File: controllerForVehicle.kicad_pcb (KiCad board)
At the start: 4 copper layers, 208 parts, among them IC1 MP2338GTL-Z, J1 Debug, J10 Conn_01x02, J11 Conn_01x02, J12 Conn_01x02, J13 USB_C_Receptacle_PowerOnly_6P, J14 USB_C_Receptacle_USB2.0_16P, J15 USB_C_Receptacle_USB2.0_16P, J2 Boot_Sel, J3 VIN, J4 Conn_01x08, J5 Conn_01x08, J6 Conn_01x08, J7 Conn_01x02, J8 Conn_01x02, J9 Conn_01x02, SW1 RESET, SW2 IO0, SW3 EN, T1 S8050, T2 S8050, U1 STM32F103C8Tx, U10 MPU6050, U11 MCP23S17_SO, U2 L298N, U3 L298N, U4 L298N, U5 ESP32-WROOM-32D, U6 CP2102N-Axx-xQFN28, U7 L7805, U8 AMS1117-3.3, U9 PCA9685PW, Y1 8mHz, Y2 32.768kHz

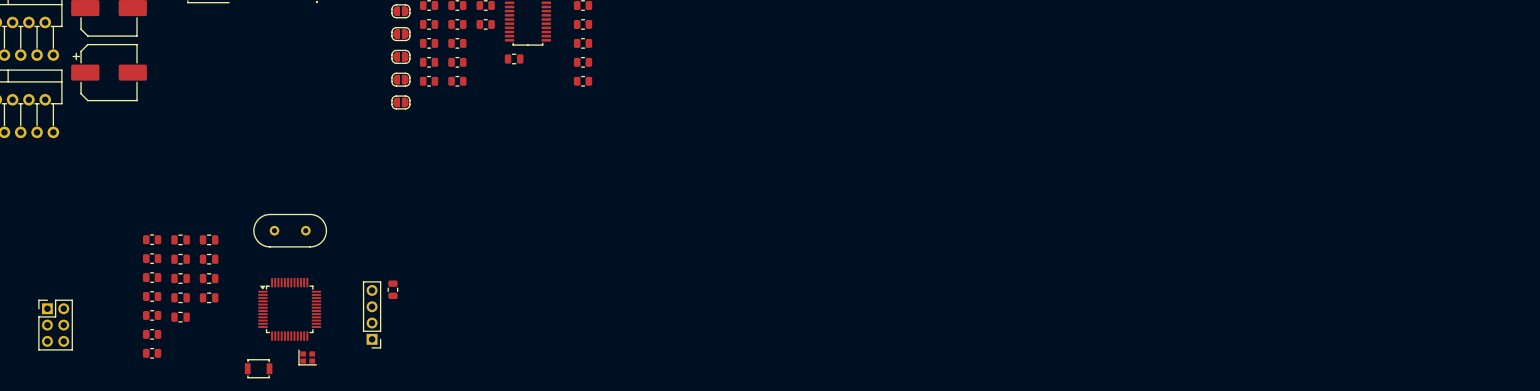
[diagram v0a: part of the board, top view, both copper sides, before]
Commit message: Routing
Routing STM32 and Components
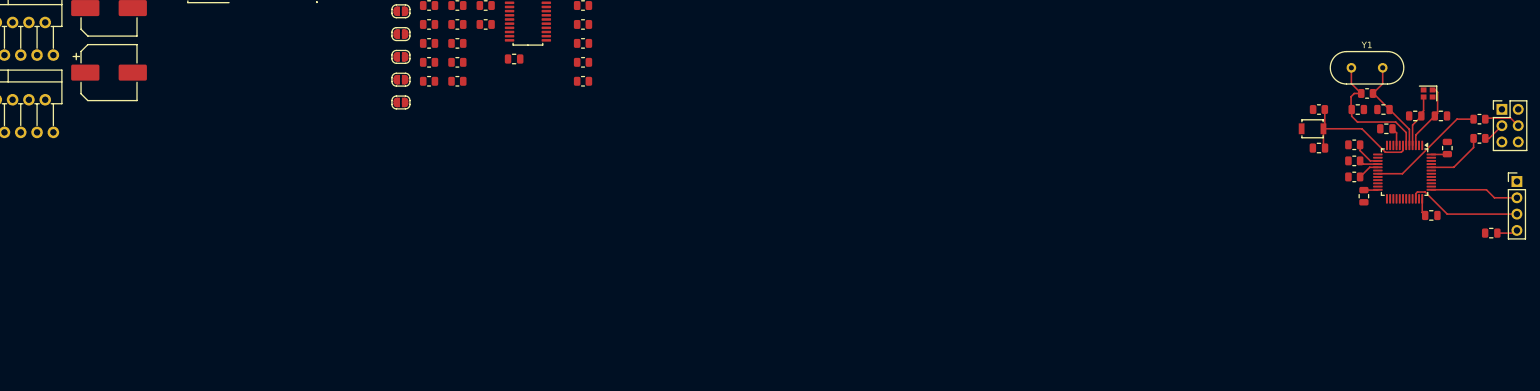
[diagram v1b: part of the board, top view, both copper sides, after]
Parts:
- Y1: footprint Crystal:Crystal_HC49-U_Vertical -> Crystal:Crystal_HC49-4H_Vertical
- moved J2 228.7 mm to (269.7, 138.2)
- moved R7 209.9 mm to (266.2, 139.8), turned to 180 degrees
- moved R6 209.0 mm to (266.2, 142.8)
- moved C5 199.1 mm to (261.2, 144.2), turned to -90 degrees
- moved C4 195.2 mm to (258.7, 154.8), turned to 180 degrees
- moved C7 193.2 mm to (260.2, 139.2)
- moved R1 190.6 mm to (248.7, 135.8), turned to 180 degrees
- moved C8 189.6 mm to (256.2, 139.2)
- moved C2 188.9 mm to (251.7, 141.2)
- moved C1 188.5 mm to (251.2, 138.2), turned to 180 degrees
- moved R4 188.2 mm to (246.7, 148.8), turned to 180 degrees
- moved R3 188.1 mm to (246.7, 146.2), turned to 180 degrees
- moved R2 188.1 mm to (246.7, 143.8), turned to 180 degrees
- moved C3 184.8 mm to (248.2, 151.8), turned to 90 degrees
- moved R5 184.6 mm to (241.2, 138.2)
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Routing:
- net OSC_OUT: track 0.00 -> 21.1 mm
- net RESET: track 0.00 -> 20.7 mm
- net BOOT1: track 0.00 -> 18.4 mm
- net SWDIO: track 0.00 -> 18.1 mm
- net OSC_IN: track 0.00 -> 15.1 mm
- net SWCLK: track 0.00 -> 13.9 mm
- net 3V3: track 0.00 -> 13.6 mm
- net PC14: track 0.00 -> 10.6 mm
- net BOOT0: track 0.00 -> 9.28 mm
- net PC15: track 0.00 -> 8.25 mm
- net Net-(J2-Pad4): track 0.00 -> 5.68 mm
- net Net-(U1-PA5): track 0.00 -> 4.33 mm
- net Net-(J2-Pad3): track 0.00 -> 3.41 mm
- net Net-(U1-PA7): track 0.00 -> 3.38 mm
- net Net-(U1-PA6): track 0.00 -> 2.97 mm

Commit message: Routing
Routing ESP32 and Components
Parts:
- removed C7, C8: 20p, Capacitor_SMD:C_0805_2012Metric
- removed Y2: 32.768kHz, Crystal:Crystal_SMD_2016-4Pin_2.0x1.6mm
- moved C16 220.6 mm to (246.0, 61.8)
- moved C19 220.5 mm to (249.8, 56.5), turned to 90 degrees
- moved C17 215.8 mm to (246.0, 59.4)
- moved C20 213.0 mm to (247.4, 56.5), turned to 90 degrees
- moved C21 209.7 mm to (245.1, 82.0)
- moved U6 203.2 mm to (242.8, 54.5), turned to 90 degrees
- moved C15 181.2 mm to (205.5, 52.5), turned to 90 degrees
- moved C14 177.3 mm to (202.0, 52.5), turned to 90 degrees
- moved C18 174.5 mm to (204.3, 61.2)
- moved R17 170.8 mm to (251.1, 36.9)
- moved R18 170.8 mm to (251.1, 39.9)
- moved U5 170.8 mm to (219.7, 58.1)
- moved SW2 169.1 mm to (245.1, 79.0), turned to 180 degrees
- moved R11 168.1 mm to (241.1, 76.0)
- moved R8 165.7 mm to (236.3, 77.1), turned to 90 degrees
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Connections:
- U1 pad 3: PC14 -> unconnected-(U1-PC14-Pad3)
- U1 pad 4: PC15 -> unconnected-(U1-PC15-Pad4)
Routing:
- net IO0: track 0.00 -> 19.0 mm
- net 3V3: track 13.6 -> 28.4 mm
- net EN: track 0.00 -> 11.1 mm
- net OSC_OUT: track 21.1 -> 10.5 mm
- net PC14: track 10.6 -> 0.00 mm
- net PC15: track 8.25 -> 0.00 mm
- net Net-(C22-Pad1): track 0.00 -> 7.13 mm
- net Net-(C21-Pad1): track 0.00 -> 6.89 mm
- net DTR: track 0.00 -> 6.13 mm
- net RTS: track 0.00 -> 5.93 mm
- net 5V1: track 0.00 -> 4.78 mm
- net Net-(T1-B): track 0.00 -> 4.76 mm
- net OSC_IN: track 15.1 -> 11.0 mm
- net Net-(U6-TXD): track 0.00 -> 3.28 mm
- net RXD: track 0.00 -> 3.24 mm
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
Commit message: Routing ESP32 and Components
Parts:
- removed R10: 470R, Resistor_SMD:R_0805_2012Metric
- removed R17: 0R (NC), Resistor_SMD:R_0805_2012Metric
- removed R18: 0R(NC), Resistor_SMD:R_0805_2012Metric
- moved J14 85.7 mm to (185.2, 80.1), turned to -90 degrees
- moved D27 82.6 mm to (193.4, 79.2), turned to -90 degrees
- moved D28 82.6 mm to (193.4, 81.0), turned to 90 degrees
- moved D26 70.8 mm to (186.4, 73.1), turned to 180 degrees
- moved R45 61.6 mm to (190.9, 81.9), turned to -90 degrees
- moved R47 60.0 mm to (190.9, 78.3), turned to 90 degrees
- moved C19 59.0 mm to (200.7, 89.2), turned to 180 degrees
- moved C16 57.3 mm to (193.8, 85.4), turned to -90 degrees
- moved R49 56.8 mm to (191.6, 75.4), turned to 180 degrees
- moved C17 56.3 mm to (196.1, 85.4), turned to -90 degrees
- moved C20 55.8 mm to (200.7, 87.0), turned to 180 degrees
- moved U6 50.3 mm to (200.9, 82.2), turned to 0 degrees
- moved R16 41.5 mm to (206.9, 82.3), turned to 0 degrees
- moved R15 35.4 mm to (206.9, 80.2), turned to 0 degrees
- moved SW2 34.7 mm to (214.0, 63.7), turned to 90 degrees
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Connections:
- U6 pad 26: Net-(U6-TXD) -> TXD
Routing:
- net EN: track 11.1 -> 41.2 mm, vias 0 -> 2
- net Net-(D26-A): track 0.00 -> 13.0 mm
- net ESP_D+: track 0.00 -> 11.7 mm
- net IO0: track 19.0 -> 29.5 mm
- net ESP_D-: track 0.00 -> 9.32 mm
- net TXD: track 1.98 -> 8.65 mm
- net Net-(J14-D--PadA7): track 0.00 -> 6.24 mm
- net Net-(J14-D+-PadA6): track 0.00 -> 6.18 mm, vias 0 -> 2
- net RXD: track 3.24 -> 9.36 mm
- net 5V1: track 4.78 -> 10.2 mm
- net Net-(T2-B): track 2.28 -> 7.00 mm
- net Net-(U6-TXD): track 3.28 -> 0.00 mm
- net RTS: track 5.93 -> 7.75 mm, vias 0 -> 2
- net Net-(C21-Pad1): track 6.89 -> 5.14 mm
- net Net-(C22-Pad1): track 7.13 -> 5.43 mm
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
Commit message: Power Routing
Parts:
- removed R62, R63, R64: 12k, Resistor_SMD:R_0805_2012Metric
- added R10: 12k, Resistor_SMD:R_0805_2012Metric, F.Cu at (-21.2, 83.8)
- added R17: 12k, Resistor_SMD:R_0805_2012Metric, F.Cu at (-21.2, 86.8)
- added R18: 12k, Resistor_SMD:R_0805_2012Metric, F.Cu at (-7.89, 73.8)
- moved C30 174.9 mm to (171.0, 236.2)
- moved C28 174.5 mm to (163.0, 235.2), turned to 180 degrees
- moved C31 174.3 mm to (171.0, 238.4)
- moved C29 170.8 mm to (166.2, 231.6), turned to 90 degrees
- moved C27 169.1 mm to (163.0, 237.6), turned to 180 degrees
- moved C33 163.6 mm to (158.7, 227.8), turned to -90 degrees
- moved R25 162.5 mm to (159.2, 235.2), turned to 180 degrees
- moved R27 159.7 mm to (159.2, 237.6), turned to 180 degrees
- moved C32 158.7 mm to (163.2, 227.8), turned to -90 degrees
- moved R26 158.4 mm to (165.8, 227.8), turned to -90 degrees
- moved R30 152.6 mm to (160.9, 227.8), turned to -90 degrees
- moved R29 152.3 mm to (156.4, 227.8), turned to -90 degrees
- moved R28 151.6 mm to (158.4, 231.0), turned to 180 degrees
- moved J3 150.4 mm to (33.8, 185.1)
- moved C23 146.3 mm to (119.8, 223.8), turned to 90 degrees
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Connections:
- R58 pad 1: DCEn6 -> Net-(U3-EnB)
- R58 pad 2: Net-(U9-LED10) -> DCEn4
- R59 pad 1: DCEn5 -> Net-(U4-EnA)
- R59 pad 2: Net-(U9-LED11) -> DCEn5
- R60 pad 1: DCEn4 -> Net-(U4-EnB)
- R60 pad 2: Net-(U9-LED12) -> DCEn6
- U2 pad 11: DCEn2 -> Net-(U2-EnB)
- U2 pad 6: DCEn1 -> Net-(U2-EnA)
- U3 pad 11: DCEn4 -> Net-(U3-EnB)
- U3 pad 6: DCEn3 -> Net-(U3-EnA)
- U4 pad 11: DCEn6 -> Net-(U4-EnB)
- U4 pad 6: DCEn5 -> Net-(U4-EnA)
- U9 pad 17: Net-(U9-LED10) -> DCEn6
- U9 pad 18: Net-(U9-LED11) -> DCEn5
- U9 pad 19: Net-(U9-LED12) -> DCEn4
- U9 pad 20: Net-(U9-LED13) -> DCEn3
- U9 pad 21: Net-(U9-LED14) -> DCEn2
- U9 pad 22: Net-(U9-LED15) -> DCEn1

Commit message: Reapply "placing completed."
This reverts commit 83f85ef5575867dc78eeeae3514badb4960c2205.
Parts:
- added C7: 220uF 35V, Capacitor_SMD:CP_Elec_8x10.5, F.Cu at (-20.6, 32.5)
- moved R55 276.9 mm to (343.0, 143.3)
- moved R83 274.5 mm to (-150.8, 52.7), turned to 90 degrees
- moved R53 273.4 mm to (339.7, 139.3), turned to -90 degrees
- moved R82 271.4 mm to (-148.2, 52.6), turned to 90 degrees
- moved R52 271.0 mm to (337.6, 139.3), turned to -90 degrees
- moved R81 267.2 mm to (-144.4, 52.4), turned to 90 degrees
- moved R80 264.3 mm to (-141.9, 52.4), turned to 90 degrees
- moved C43 255.7 mm to (334.1, 137.8), turned to 180 degrees
- moved U9 249.6 mm to (331.9, 144.3)
- moved J8 238.8 mm to (-150.2, 39.1), turned to 180 degrees
- moved R79 234.6 mm to (-113.0, 50.7), turned to 90 degrees
- moved R78 231.4 mm to (-110.4, 50.7), turned to 90 degrees
- moved R68 230.4 mm to (339.3, 120.8), turned to 90 degrees
- moved JP7 229.1 mm to (340.0, 116.5), turned to -90 degrees
- moved R72 227.0 mm to (337.2, 120.8), turned to 90 degrees
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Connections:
- J9 pad 1: DC5_2 -> DC4_2
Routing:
- net DC2_1: track 0.00 -> 18.9 mm
- net DC2_2: track 0.00 -> 14.6 mm
- net DCIn6_1: track 0.00 -> 14.1 mm
- net DCIn6_2: track 0.00 -> 14.0 mm
- net Net-(U4-EnA): track 0.00 -> 10.4 mm
- net DCIn5_2: track 0.00 -> 9.16 mm
- net Net-(U2-EnA): track 0.00 -> 9.10 mm
- net DCIn1_2: track 0.00 -> 7.60 mm
- net DCIn1_1: track 0.00 -> 7.58 mm
- net Net-(U4-EnB): track 0.00 -> 5.49 mm

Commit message: silinecek
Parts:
- removed D32, D33, D34, D35, D36, D37, D38, D39: 1N4007, Diode_SMD:D_SOD-123
- removed R82, R83: 100R, Resistor_SMD:R_0805_2012Metric
- removed R84: 10K, Resistor_SMD:R_0805_2012Metric
- added C8: 0.1u, Capacitor_SMD:C_0805_2012Metric, F.Cu at (-17.1, 7.30)
- added D17: 1N4007, Diode_SMD:D_SOD-123, F.Cu at (-30.6, -20.7)
- added D18: 1N4007, Diode_SMD:D_SOD-123, F.Cu at (-30.6, -17.4)
- added D19: 1N4007, Diode_SMD:D_SOD-123, F.Cu at (-30.6, -14.0)
- added D20: 1N4007, Diode_SMD:D_SOD-123, F.Cu at (-30.6, -10.7)
- added D21: 1N4007, Diode_SMD:D_SOD-123, F.Cu at (-30.6, -7.33)
- added D22: 1N4007, Diode_SMD:D_SOD-123, F.Cu at (-30.6, -3.98)
- added D23: 1N4007, Diode_SMD:D_SOD-123, F.Cu at (-30.6, -0.62)
- added D24: 1N4007, Diode_SMD:D_SOD-123, F.Cu at (-30.6, 2.73)
- added J16: Servo6, Connector_JST:JST_XA_B03B-XASK-1_1x03_P2.50mm_Vertical, F.Cu at (105.1, 38.6)
- added J17: Servo8, Connector_JST:JST_XA_B03B-XASK-1_1x03_P2.50mm_Vertical, F.Cu at (105.2, 61.4)
- added J18: USB_C_Receptacle_PowerOnly_6P, Connector_USB:USB_C_Receptacle_GCT_USB4125-xx-x_6P_TopMnt_Horizontal, F.Cu at (-8.29, -0.62)
- added J19: USB_C_Receptacle_USB2.0_16P, Connector_USB:USB_C_Receptacle_Palconn_UTC16-G, F.Cu at (-20.0, -18.3)
- added J20: USB_C_Receptacle_USB2.0_16P, Connector_USB:USB_C_Receptacle_Palconn_UTC16-G, F.Cu at (-20.0, -8.30)
- added R62: 10k, Resistor_SMD:R_0805_2012Metric, F.Cu at (36.0, 20.0)
- added R63: 10k, Resistor_SMD:R_0805_2012Metric, F.Cu at (-23.6, 7.28)
- added R64: 10k, Resistor_SMD:R_0805_2012Metric, F.Cu at (-23.6, 10.2)
- C10: value 0.1u -> 220uF 35V; footprint Capacitor_SMD:C_0805_2012Metric -> Capacitor_SMD:CP_Elec_8x10.5
- C12: value 220uF 35V -> 100u; footprint Capacitor_SMD:CP_Elec_8x10.5 -> Capacitor_SMD:C_0805_2012Metric
- C13: value 220uF 35V -> 0.1u; footprint Capacitor_SMD:CP_Elec_8x10.5 -> Capacitor_SMD:C_0805_2012Metric
- C14: value 100u -> 10u
- C16, C19: value 10u -> 1n / 50V
- C17: value 0.1u -> 10u
- C18: value 1n / 50V -> 0.1u
- C20: value 0.1u -> 1n / 50V
- C21, C22: value 1n / 50V -> 10u
- C25: value 10u -> 22u
- C26: value 10u -> 0.1u
- C27: value 22u -> 0.1u
- C28, C29: value 0.1u -> 22u
- C30: value 22u -> 22n
- C31: value 22u -> 300p
- C32: value 22n -> 0.01u
- C33: value 300p -> 47u
- C34: value 0.01u -> 47u
- C35, C36: value 47u -> 4.7u
- C37: value 4.7u -> 0.01u
- C38: value 4.7u -> 2200p
- C39: value 0.01u -> 22p
- C40: value 2200p -> 0.01u
- C41: value 22p -> 220uF 35V; footprint Capacitor_SMD:C_0805_2012Metric -> Capacitor_SMD:CP_Elec_8x10.5
- C42: value 0.01u -> 220uF 35V; footprint Capacitor_SMD:C_0805_2012Metric -> Capacitor_SMD:CP_Elec_8x10.5
- C7: value 220uF 35V -> 1uf; footprint Capacitor_SMD:CP_Elec_8x10.5 -> Capacitor_SMD:C_0805_2012Metric
- C9: value 1uf -> 220uF 35V; footprint Capacitor_SMD:C_0805_2012Metric -> Capacitor_SMD:CP_Elec_8x10.5
- D27: value ESD05V88D-LC -> 1N5819; footprint Diode_SMD:D_SOD-882 -> Diode_SMD:D_SOD-123
- D31: value 1N5819 -> ESD05V88D-LC; footprint Diode_SMD:D_SOD-123 -> Diode_SMD:D_SOD-882
- J10, J11, J12, J8, J9: footprint Connector_JST:JST_XH_S2B-XH-A-1_1x02_P2.50mm_Horizontal -> Connector_JST:JST_XH_B2B-XH-A_1x02_P2.50mm_Vertical
- J13: value USB_C_Receptacle_PowerOnly_6P -> Conn_01x02; footprint Connector_USB:USB_C_Receptacle_GCT_USB4125-xx-x_6P_TopMnt_Horizontal -> Connector_JST:JST_XH_B2B-XH-A_1x02_P2.50mm_Vertical
- J14: value USB_C_Receptacle_USB2.0_16P -> Servo2; footprint Connector_USB:USB_C_Receptacle_Palconn_UTC16-G -> Connector_JST:JST_XA_B03B-XASK-1_1x03_P2.50mm_Vertical
- J15: value USB_C_Receptacle_USB2.0_16P -> Servo4; footprint Connector_USB:USB_C_Receptacle_Palconn_UTC16-G -> Connector_JST:JST_XA_B03B-XASK-1_1x03_P2.50mm_Vertical
- J3: value VIN -> Servo1; footprint Connector_AMASS:AMASS_XT60PW-F_1x02_P7.20mm_Horizontal -> Connector_JST:JST_XA_B03B-XASK-1_1x03_P2.50mm_Vertical
- J4: value Conn_01x08 -> Servo3; footprint Connector_PinHeader_2.54mm:PinHeader_1x08_P2.54mm_Vertical -> Connector_JST:JST_XA_B03B-XASK-1_1x03_P2.50mm_Vertical
- J5: value Conn_01x08 -> Servo5; footprint Connector_PinHeader_2.54mm:PinHeader_1x08_P2.54mm_Vertical -> Connector_JST:JST_XA_B03B-XASK-1_1x03_P2.50mm_Vertical
- J6: value Conn_01x08 -> Servo7; footprint Connector_PinHeader_2.54mm:PinHeader_1x08_P2.54mm_Vertical -> Connector_JST:JST_XA_B03B-XASK-1_1x03_P2.50mm_Vertical
- J7: value Conn_01x02 -> VIN; footprint Connector_JST:JST_XH_S2B-XH-A-1_1x02_P2.50mm_Horizontal -> Connector_AMASS:AMASS_XT60PW-F_1x02_P7.20mm_Horizontal
- R11: value 470R -> 12k
- R12, R13: value 12K -> 12k
- R14: value 470R -> 5K
- R15: value 0R -> 12k
- R16: value 0R -> 470R
- R17, R18: value 12k -> 12K
- R19: value 22R -> 470R
- R20: value 22R -> 0R
- R21: value 100R -> 0R
- R22: value 100R -> 22R
- R23: value 0R -> 22R
- R24: value 0R -> 100R
- R25: value 191K -> 100R
- R26: value 10K -> 0R
- R27: value 49.9K -> 0R
- R28: value 10K -> 191K
- R29: value 90.9k -> 10K
- R30: value 10K -> 49.9K
- R31: value 51.1 -> 10K
- R32: value 665K -> 90.9k
- R33: value 10.2k -> 10K
- R34: value 130K -> 51.1
- R35: value 37.4k -> 665K
- R36: value 1.96k -> 10.2k
- R37: value 12k -> 130K
- R38: value 12k -> 37.4k
- R39: value 12k -> 1.96k
- R45, R46, R47: value 20R -> 12k
- R49, R50: value 4.7K -> 20R
- R51: value 10k -> 20R
- R52, R53, R66: value 10k -> 4.7K
- R58, R59, R60: value 12k -> 10k
- R67, R68, R72: value 10k -> 100R
- R69: value 4.7K -> 10k
- R74: value 100R -> 10k
- R77: value 10k -> 10K
- R8: value 5K -> 12k
- moved C21 428.0 mm to (-127.4, 317.1)
- moved C22 428.0 mm to (-159.9, 317.1)
- moved R55 316.1 mm to (48.7, 27.9), turned to 180 degrees
- moved JP6 313.5 mm to (35.9, 16.5), turned to -90 degrees
- moved R61 311.7 mm to (38.7, 20.0), turned to 90 degrees
- moved JP5 309.9 mm to (38.7, 16.5), turned to -90 degrees
- moved U9 309.8 mm to (42.8, 33.1)
- moved C43 309.8 mm to (44.9, 26.8)
- moved JP4 306.2 mm to (41.4, 16.5), turned to -90 degrees
- moved R57 303.0 mm to (47.0, 20.0), turned to 90 degrees
- moved JP3 302.6 mm to (44.2, 16.5), turned to -90 degrees
- moved JP2 298.9 mm to (46.9, 16.5), turned to -90 degrees
- moved R54 298.1 mm to (49.9, 20.0), turned to 90 degrees
- moved R56 296.3 mm to (48.7, 30.0)
- moved JP1 295.3 mm to (49.7, 16.5), turned to -90 degrees
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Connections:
- C10 pad 1: GND -> VIN
- C10 pad 2: 3V3 -> GND
- C12 pad 1: VIN -> GND
- C12 pad 2: GND -> 3V3
- C13 pad 1: VIN -> GND
- C13 pad 2: GND -> 3V3
- C14 pad 1: GND -> 3V3
- C14 pad 2: 3V3 -> GND
- C15 pad 1: GND -> 3V3
- C15 pad 2: 3V3 -> GND
- C16 pad 1: 3V3 -> GND
- C16 pad 2: GND -> EN
- C17 pad 1: 3V3 -> GND
- C17 pad 2: GND -> 5V1
- C18 pad 2: EN -> 5V1
- C19 pad 1: GND -> Net-(C19-Pad1)
- C19 pad 2: 5V1 -> GND
- C20 pad 1: GND -> Net-(C20-Pad1)
- C20 pad 2: 5V1 -> GND
- C21 pad 1: Net-(C21-Pad1) -> GND
- C21 pad 2: GND -> VIN
- C22 pad 1: Net-(C22-Pad1) -> GND
- C22 pad 2: GND -> 5V1
- C23 pad 2: VIN -> 5V1
- C24 pad 2: 5V1 -> 3V3
- C25 pad 2: 5V1 -> VIN
- C26 pad 2: 3V3 -> VIN
- C27 pad 1: GND -> Net-(IC1-SW)
- C27 pad 2: VIN -> Net-(IC1-BST)
- C28 pad 2: VIN -> 5V2
- C29 pad 1: Net-(IC1-SW) -> GND
- C29 pad 2: Net-(IC1-BST) -> 5V2
- C30 pad 2: 5V2 -> Net-(IC1-SS)
- C31 pad 1: GND -> 5V2
- C31 pad 2: 5V2 -> Net-(C31-Pad2)
- C32 pad 1: GND -> Net-(PS1-BOOT)
- C32 pad 2: Net-(IC1-SS) -> Net-(D25-K)
- C33 pad 1: 5V2 -> GND
- C33 pad 2: Net-(C33-Pad2) -> 5VRPi
- C34 pad 1: Net-(PS1-BOOT) -> GND
- C34 pad 2: Net-(D25-K) -> 5VRPi
- C35 pad 2: 5VRPi -> VIN
- C36 pad 2: 5VRPi -> VIN
- C38 pad 1: GND -> Net-(C38-Pad1)
- C38 pad 2: VIN -> Net-(PS1-COMP)
- C39 pad 2: VIN -> Net-(PS1-COMP)
- C40 pad 1: Net-(C40-Pad1) -> GND
- C40 pad 2: Net-(PS1-COMP) -> Net-(PS1-SS)
- C41 pad 1: GND -> 5V2
- C41 pad 2: Net-(PS1-COMP) -> GND
- C42 pad 1: GND -> 5V2
- C42 pad 2: Net-(PS1-SS) -> GND
- C7 pad 1: 5V2 -> GND
- C7 pad 2: GND -> RESET
- C9 pad 1: GND -> VIN
- C9 pad 2: RESET -> GND
- D13 pad 1: DC5_1 -> DC3_1
- D14 pad 1: DC5_2 -> DC3_2
- D15 pad 1: DC6_1 -> DC4_1
- D16 pad 1: DC6_2 -> DC5_2
- D27 pad 1: GND -> 5V1
- D27 pad 2: ESP_D+ -> Net-(D27-A)
- D28 pad 2: ESP_D- -> USB_D-
- D30 pad 2: USB_D- -> ESP_D+
- D31 pad 1: 5V1 -> GND
- D31 pad 2: Net-(D31-A) -> ESP_D-
- D5 pad 2: DC5_1 -> DC3_1
- D6 pad 2: DC5_2 -> DC3_2
- D7 pad 2: DC6_1 -> DC4_1
- D8 pad 2: DC6_2 -> DC5_2
- J10 pad 1: DC3_2 -> DC4_2
- J10 pad 2: DC3_1 -> DC4_1
- J11 pad 1: DC2_2 -> DC3_2
- J11 pad 2: DC2_1 -> DC3_1
- J12 pad 1: DC1_2 -> DC2_2
- J12 pad 2: DC1_1 -> DC2_1
- J3 pad 1: VIN -> GND
- J3 pad 2: GND -> 5V2
- J4 pad 1: Net-(J4-Pin_1) -> GND
- J4 pad 2: Net-(J4-Pin_2) -> 5V2
- J5 pad 1: 5V2 -> GND
- J5 pad 3: 5V2 -> Net-(J5-Pin_3)
- J6 pad 2: GND -> 5V2
- J6 pad 3: GND -> Net-(J6-Pin_3)
- J7 pad 1: DC6_2 -> VIN
- J7 pad 2: DC6_1 -> GND
- J8 pad 1: DC5_2 -> DC6_2
- J8 pad 2: DC5_1 -> DC6_1
- J9 pad 1: DC4_2 -> DC5_2
- J9 pad 2: DC4_1 -> DC5_1
- R10 pad 1: Net-(U2-EnA) -> Net-(U2-EnB)
- R10 pad 2: DCEn1 -> DCEn2
- R11 pad 1: IO0 -> Net-(U3-EnB)
- R11 pad 2: Net-(C21-Pad1) -> DCEn4
- R12 pad 1: Net-(T1-B) -> Net-(U4-EnA)
- R12 pad 2: DTR -> DCEn5
- R13 pad 1: Net-(T2-B) -> Net-(U4-EnB)
- R13 pad 2: RTS -> DCEn6
- R14 pad 1: EN -> 3V3
- R14 pad 2: Net-(C22-Pad1) -> IO0
- R15 pad 1: TXD -> EN
- R15 pad 2: RXD0 -> 3V3
- R16 pad 1: RXD -> IO0
- R16 pad 2: TXD0 -> Net-(C19-Pad1)
- R17 pad 1: Net-(U2-EnB) -> Net-(T1-B)
- R17 pad 2: DCEn2 -> DTR
- R18 pad 1: Net-(U3-EnA) -> Net-(T2-B)
- R18 pad 2: DCEn3 -> RTS
- R19 pad 1: TXD1 -> EN
- R19 pad 2: USART1_RX -> Net-(C20-Pad1)
- R20 pad 1: RXD1 -> TXD
- R20 pad 2: USART1_TX -> RXD0
- R21 pad 1: I2C1_SCL -> RXD
- R21 pad 2: PCA_SCL -> TXD0
- R22 pad 1: I2C1_SDA -> TXD1
- R22 pad 2: PCA_SDA -> USART1_RX
- R23 pad 1: I2C2_SDA -> RXD1
- R23 pad 2: MPU_SDA -> USART1_TX
- R24 pad 1: I2C2_SCL -> I2C1_SCL
- R24 pad 2: MPU_SCL -> PCA_SCL
- R25 pad 1: VIN -> I2C1_SDA
- R25 pad 2: Net-(IC1-EN) -> PCA_SDA
- R26 pad 1: 5V2 -> I2C2_SDA
- R26 pad 2: Net-(IC1-PG) -> MPU_SDA
- R27 pad 1: Net-(IC1-EN) -> I2C2_SCL
- R27 pad 2: GND -> MPU_SCL
- R28 pad 1: Net-(IC1-FB) -> VIN
- R28 pad 2: Net-(C33-Pad2) -> Net-(IC1-EN)
- R29 pad 2: Net-(C33-Pad2) -> Net-(IC1-PG)
- R30 pad 1: GND -> Net-(IC1-EN)
- R30 pad 2: Net-(C33-Pad2) -> GND
- R31 pad 1: 5VRPi -> Net-(IC1-FB)
- R31 pad 2: Net-(R31-Pad2) -> Net-(C31-Pad2)
- R32 pad 1: VIN -> 5V2
- R32 pad 2: Net-(PS1-EN) -> Net-(C31-Pad2)
- R33 pad 1: Net-(R31-Pad2) -> GND
- R33 pad 2: Net-(PS1-VSENSE) -> Net-(C31-Pad2)
- R34 pad 1: Net-(PS1-EN) -> 5VRPi
- R34 pad 2: GND -> Net-(R34-Pad2)
- R35 pad 1: Net-(C40-Pad1) -> VIN
- R35 pad 2: GND -> Net-(PS1-EN)
- R36 pad 1: Net-(PS1-VSENSE) -> Net-(R34-Pad2)
- R36 pad 2: GND -> Net-(PS1-VSENSE)
- R37 pad 1: Net-(J4-Pin_1) -> Net-(PS1-EN)
- R37 pad 2: PCA_0 -> GND
- R38 pad 1: Net-(J4-Pin_2) -> Net-(C38-Pad1)
- R38 pad 2: PCA_1 -> GND
- R39 pad 1: Net-(J4-Pin_3) -> Net-(PS1-VSENSE)
- R39 pad 2: PCA_2 -> GND
- R40 pad 1: Net-(J4-Pin_4) -> Net-(J3-Pin_3)
- R40 pad 2: PCA_3 -> PCA_0
- R41 pad 1: Net-(J4-Pin_5) -> Net-(J4-Pin_3)
- R41 pad 2: PCA_4 -> PCA_2
- R42 pad 1: Net-(J4-Pin_6) -> Net-(J5-Pin_3)
- R42 pad 2: PCA_5 -> PCA_4
- R43 pad 1: Net-(J4-Pin_7) -> Net-(J6-Pin_3)
- R44 pad 1: Net-(J4-Pin_8) -> Net-(J14-Pin_3)
- R44 pad 2: PCA_7 -> PCA_1
- R45 pad 1: Net-(J14-D--PadA7) -> Net-(J15-Pin_3)
- R45 pad 2: ESP_D- -> PCA_3
- R46 pad 1: Net-(J15-D--PadA7) -> Net-(J16-Pin_3)
- R46 pad 2: USB_D- -> PCA_5
- R47 pad 1: Net-(J14-D+-PadA6) -> Net-(J17-Pin_3)
- R47 pad 2: ESP_D+ -> PCA_7
- R48 pad 1: Net-(J15-D+-PadA6) -> Net-(J19-D--PadA7)
- R48 pad 2: USB_D+ -> USB_D-
- R49 pad 1: 5V1 -> Net-(J20-D--PadA7)
- R49 pad 2: ESP_D+ -> ESP_D-
- R50 pad 1: 5V1 -> Net-(J19-D+-PadA6)
- R51 pad 1: GND -> Net-(J20-D+-PadA6)
- R51 pad 2: PCA_A0 -> ESP_D+
- R52 pad 1: 3V3 -> 5V1
- R52 pad 2: PCA_SDA -> USB_D+
- R53 pad 1: 3V3 -> 5V1
- R53 pad 2: PCA_SCL -> ESP_D+
- R54 pad 2: PCA_A1 -> PCA_A0
- R55 pad 1: OE -> 3V3
- R55 pad 2: GND -> PCA_SDA
- R56 pad 1: GND -> 3V3
- R56 pad 2: PCA_A2 -> PCA_SCL
- R57 pad 2: PCA_A3 -> PCA_A1
- R58 pad 1: Net-(U3-EnB) -> OE
- R58 pad 2: DCEn4 -> GND
- R59 pad 1: Net-(U4-EnA) -> GND
- R59 pad 2: DCEn5 -> PCA_A2
- R60 pad 1: Net-(U4-EnB) -> GND
- R60 pad 2: DCEn6 -> PCA_A3
- R65 pad 2: PCA_A5 -> MCP_A0
- R66 pad 1: MPU_SCL -> 3V3
- R66 pad 2: 3V3 -> SPI1_CS
- R67 pad 1: 3V3 -> DCIn1_1
- R67 pad 2: MPU_SDA -> Net-(U11-GPB0)
- R68 pad 1: GND -> DCIn1_2
- R68 pad 2: MCP_A0 -> Net-(U11-GPB1)
- R69 pad 1: 3V3 -> GND
- R69 pad 2: SPI1_CS -> MCP_A1
- R70 pad 1: DCIn1_1 -> DCIn2_1
- R70 pad 2: Net-(U11-GPB0) -> Net-(U11-GPB2)
- R71 pad 1: DCIn1_2 -> DCIn2_2
- R71 pad 2: Net-(U11-GPB1) -> Net-(U11-GPB3)
- R72 pad 1: GND -> DCIn3_1
- R72 pad 2: MCP_A1 -> Net-(U11-GPB4)
- R73 pad 1: DCIn2_1 -> DCIn3_2
- R73 pad 2: Net-(U11-GPB2) -> Net-(U11-GPB5)
- R74 pad 1: DCIn2_2 -> GND
- R74 pad 2: Net-(U11-GPB3) -> MCP_A2
- R75 pad 1: DCIn3_1 -> DCIn4_1
- R75 pad 2: Net-(U11-GPB4) -> Net-(U11-GPB6)
- R76 pad 1: DCIn3_2 -> DCIn4_2
- R76 pad 2: Net-(U11-GPB5) -> Net-(U11-GPB7)
- R77 pad 1: GND -> 3V3
- R77 pad 2: MCP_A2 -> Net-(U11-~{RESET})
- R78 pad 1: DCIn4_1 -> DCIn5_1
- R78 pad 2: Net-(U11-GPB6) -> Net-(U11-GPA0)
- R79 pad 1: DCIn4_2 -> DCIn5_2
- R79 pad 2: Net-(U11-GPB7) -> Net-(U11-GPA1)
- R8 pad 1: 3V3 -> Net-(U2-EnA)
- R8 pad 2: IO0 -> DCEn1
- R80 pad 1: DCIn5_1 -> DCIn6_1
- R80 pad 2: Net-(U11-GPA0) -> Net-(U11-GPA2)
- R81 pad 1: DCIn5_2 -> DCIn6_2
- R81 pad 2: Net-(U11-GPA1) -> Net-(U11-GPA3)
- R9 pad 1: EN -> Net-(U3-EnA)
- R9 pad 2: 3V3 -> DCEn3
- SW2 pad 2: Net-(C21-Pad1) -> Net-(C19-Pad1)
- SW3 pad 2: Net-(C22-Pad1) -> Net-(C20-Pad1)
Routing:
- net 5V2: track 0.00 -> 115.0 mm
- net PCA_7: track 0.00 -> 80.6 mm, vias 0 -> 2
- net PCA_6: track 0.00 -> 70.2 mm, vias 0 -> 2
- net PCA_5: track 0.00 -> 62.1 mm, vias 0 -> 2
- net PCA_4: track 0.00 -> 58.3 mm, vias 0 -> 2
- net PCA_3: track 0.00 -> 32.7 mm
- net PCA_A0: track 0.00 -> 23.1 mm
- net PCA_2: track 0.00 -> 22.6 mm
- net PCA_A2: track 0.00 -> 20.1 mm
- net 3V3: track 28.2 -> 48.2 mm, vias 0 -> 1
- net PCA_A1: track 0.00 -> 18.9 mm
- net PCA_A4: track 0.00 -> 17.5 mm
- net PCA_A3: track 0.00 -> 16.7 mm
- net PCA_1: track 0.00 -> 12.2 mm
- net PCA_0: track 0.00 -> 11.1 mm
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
